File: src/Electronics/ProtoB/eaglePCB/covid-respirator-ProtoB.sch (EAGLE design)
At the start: 18 parts, among them IC2 L7805CV-DG, Q1 VNP35N07-E, T2 BC548

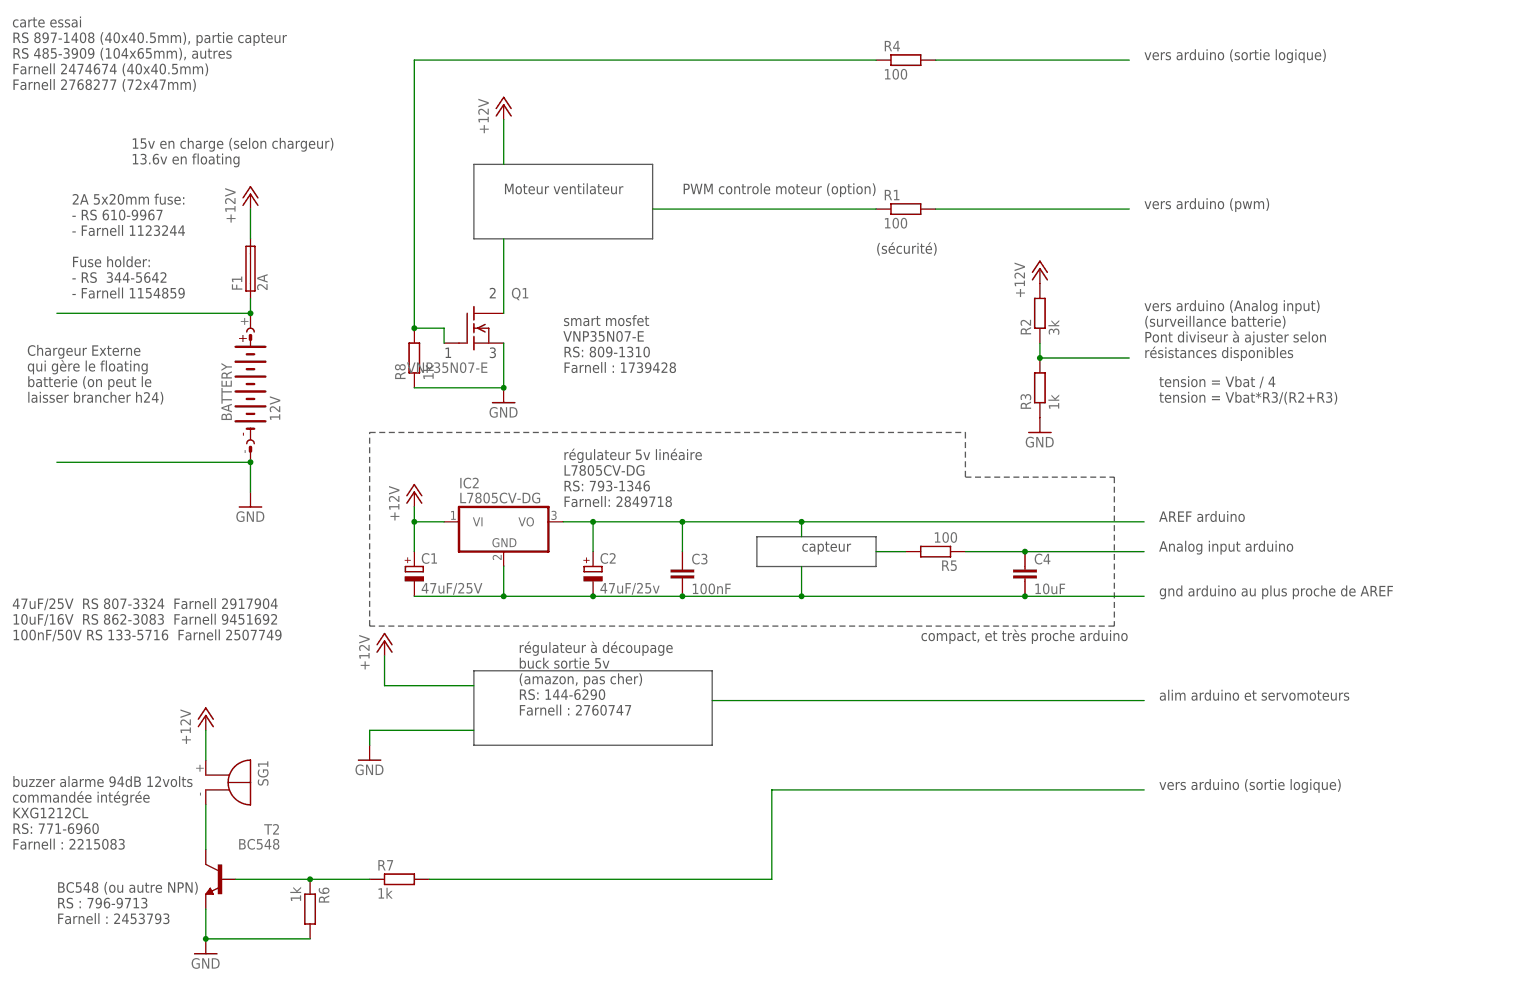
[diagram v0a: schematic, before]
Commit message: update protoB schematic
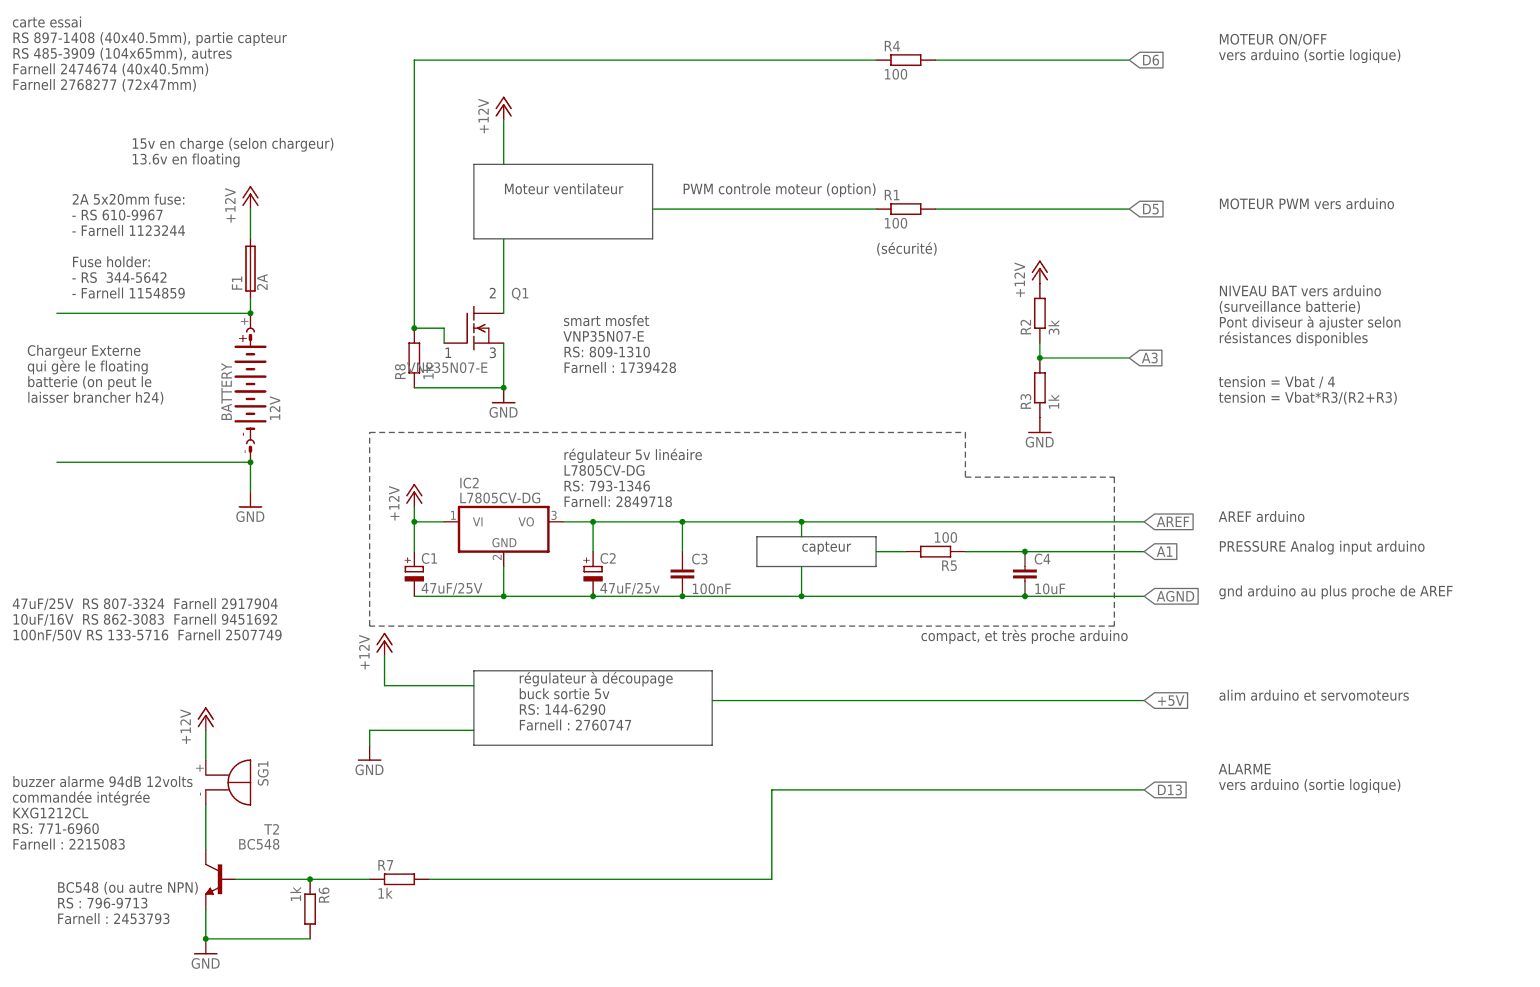
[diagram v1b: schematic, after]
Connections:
- net N$10 renamed A1
- net N$14 renamed D13
- net N$2 renamed D5
- net N$3 renamed A3
- net N$5 renamed D6
- net N$7 renamed AREF
- net N$8 renamed AGND
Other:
- note added: "ALARME vers arduino (sortie logique)"
- note added: "MOTEUR ON/OFF vers arduino (sortie logique)"
- note added: "MOTEUR PWM vers arduino"
- note added: "NIVEAU BAT vers arduino (surveillance batterie) Pont diviseur à ajuster selon résistances disponibles"
- note added: "PRESSURE Analog input arduino"
- note added: "régulateur à découpage buck sortie 5v RS: 144-6290 Farnell : 2760747"
- note removed: "Analog input arduino"
- note removed: "régulateur à découpage buck sortie 5v (amazon, pas cher) RS: 144-6290 Farnell : 2760747"
- note removed: "vers arduino (Analog input) (surveillance batterie) Pont diviseur à ajuster selon résistances disponibles"
- note removed: "vers arduino (pwm)"
- note removed: "vers arduino (sortie logique)"
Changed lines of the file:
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@@
 <text x="73.66" y="83.82" size="1.778" layer="97">PWM controle moteur (option)</text>
 <text x="106.68" y="73.66" size="1.778" layer="97">(sécurité)</text>
-<text x="152.4" y="81.28" size="1.778" layer="97">vers arduino (pwm)</text>
-<text x="152.4" y="55.88" size="1.778" layer="97">vers arduino (Analog input)
+<text x="165.1" y="81.28" size="1.778" layer="97">MOTEUR PWM vers arduino </text>
+<text x="165.1" y="58.42" size="1.778" layer="97">NIVEAU BAT vers arduino
 (surveillance batterie)
 Pont diviseur à ajuster selon
 résistances disponibles</text>
-<text x="154.94" y="48.26" size="1.778" layer="97">tension = Vbat / 4
+<text x="165.1" y="48.26" size="1.778" layer="97">tension = Vbat / 4
 tension = Vbat*R3/(R2+R3)</text>
 <text x="-20.32" y="88.9" size="1.778" layer="97">15v en charge (selon chargeur)
 13.6v en floating</text>
-<text x="152.4" y="106.68" size="1.778" layer="97">vers arduino (sortie logique)</text>
+<text x="165.1" y="106.68" size="1.778" layer="97">MOTEUR ON/OFF
+vers arduino (sortie logique)</text>
 <wire x1="86.36" y1="25.4" x2="106.68" y2="25.4" width="0.1524" layer="97"/>
 <wire x1="106.68" y1="25.4" x2="106.68" y2="20.32" width="0.1524" layer="97"/>
@@
 <wire x1="86.36" y1="20.32" x2="86.36" y2="25.4" width="0.1524" layer="97"/>
 <text x="93.98" y="22.86" size="1.778" layer="97">capteur</text>
-<text x="154.94" y="27.94" size="1.778" layer="97">AREF arduino</text>
-<text x="154.94" y="22.86" size="1.778" layer="97">Analog input arduino</text>
-<text x="154.94" y="15.24" size="1.778" layer="97">gnd arduino au plus proche de AREF</text>
+<text x="165.1" y="27.94" size="1.778" layer="97">AREF arduino</text>
+<text x="165.1" y="22.86" size="1.778" layer="97">PRESSURE Analog input arduino</text>
+<text x="165.1" y="15.24" size="1.778" layer="97">gnd arduino au plus proche de AREF</text>
 <wire x1="38.1" y1="2.54" x2="78.74" y2="2.54" width="0.1524" layer="97"/>
 <wire x1="78.74" y1="2.54" x2="78.74" y2="-10.16" width="0.1524" layer="97"/>
 <wire x1="78.74" y1="-10.16" x2="38.1" y2="-10.16" width="0.1524" layer="97"/>
 <wire x1="38.1" y1="-10.16" x2="38.1" y2="2.54" width="0.1524" layer="97"/>
-<text x="45.72" y="-5.08" size="1.778" layer="97">régulateur à découpage
+<text x="45.72" y="-7.62" size="1.778" layer="97">régulateur à découpage
 buck sortie 5v
-(amazon, pas cher)
 RS: 144-6290
 Farnell : 2760747</text>
-<text x="154.94" y="-2.54" size="1.778" layer="97">alim arduino et servomoteurs</text>
+<text x="165.1" y="-2.54" size="1.778" layer="97">alim arduino et servomoteurs</text>
 <text x="53.34" y="53.34" size="1.778" layer="97">smart mosfet
 VNP35N07-E
@@
 RS: 771-6960
 Farnell : 2215083</text>
-<text x="154.94" y="-17.78" size="1.778" layer="97">vers arduino (sortie logique)</text>
+<text x="165.1" y="-17.78" size="1.778" layer="97">ALARME
+vers arduino (sortie logique)</text>
 <text x="-33.02" y="-40.64" size="1.778" layer="97">BC548 (ou autre NPN)
 RS : 796-9713
@@
 </segment>
 </net>
-<net name="N$2" class="0">
+<net name="D5" class="0">
 <segment>
 <pinref part="R1" gate="G$1" pin="2"/>
 <wire x1="116.84" y1="81.28" x2="149.86" y2="81.28" width="0.1524" layer="91"/>
-</segment>
-</net>
-<net name="N$3" class="0">
+<label x="149.86" y="81.28" size="1.778" layer="95" xref="yes"/>
+</segment>
+</net>
+<net name="A3" class="0">
 <segment>
 <pinref part="R2" gate="G$1" pin="1"/>
@@
 <wire x1="134.62" y1="55.88" x2="149.86" y2="55.88" width="0.1524" layer="91"/>
 <junction x="134.62" y="55.88"/>
+<label x="149.86" y="55.88" size="1.778" layer="95" xref="yes"/>
 </segment>
 </net>
@@
 </segment>
 </net>
-<net name="N$5" class="0">
+<net name="D6" class="0">
 <segment>
 <pinref part="R4" gate="G$1" pin="2"/>
 <wire x1="116.84" y1="106.68" x2="149.86" y2="106.68" width="0.1524" layer="91"/>
-</segment>
-</net>
-<net name="N$7" class="0">
+<label x="149.86" y="106.68" size="1.778" layer="95" xref="yes"/>
+</segment>
+</net>
+<net name="AREF" class="0">
 <segment>
 <pinref part="IC2" gate="A1" pin="VO"/>
@@
 <wire x1="93.98" y1="27.94" x2="152.4" y2="27.94" width="0.1524" layer="91"/>
 <junction x="93.98" y="27.94"/>
-</segment>
-</net>
-<net name="N$8" class="0">
+<label x="152.4" y="27.94" size="1.778" layer="95" xref="yes"/>
+</segment>
+</net>
+<net name="AGND" class="0">
 <segment>
 <pinref part="C1" gate="G$1" pin="-"/>
@@
 <wire x1="132.08" y1="15.24" x2="152.4" y2="15.24" width="0.1524" layer="91"/>
 <junction x="132.08" y="15.24"/>
+<label x="152.4" y="15.24" size="1.778" layer="95" xref="yes"/>
 </segment>
 </net>
@@
 </segment>
 </net>
-<net name="N$10" class="0">
+<net name="A1" class="0">
 <segment>
 <pinref part="R5" gate="G$1" pin="1"/>
@@
 <wire x1="132.08" y1="22.86" x2="152.4" y2="22.86" width="0.1524" layer="91"/>
 <junction x="132.08" y="22.86"/>
-</segment>
-</net>
-<net name="N$11" class="0">
+<label x="152.4" y="22.86" size="1.778" layer="95" xref="yes"/>
+</segment>
+</net>
+<net name="+5V" class="0">
 <segment>
 <wire x1="78.74" y1="-2.54" x2="152.4" y2="-2.54" width="0.1524" layer="91"/>
+<label x="152.4" y="-2.54" size="1.778" layer="95" xref="yes"/>
 </segment>
 </net>
@@
 </segment>
 </net>
-<net name="N$14" class="0">
+<net name="D13" class="0">
 <segment>
 <pinref part="R7" gate="G$1" pin="2"/>
@@
 <wire x1="88.9" y1="-33.02" x2="88.9" y2="-17.78" width="0.1524" layer="91"/>
 <wire x1="88.9" y1="-17.78" x2="152.4" y2="-17.78" width="0.1524" layer="91"/>
-</segment>
-</net>
+<label x="152.4" y="-17.78" size="1.778" layer="95" xref="yes"/>
+</segment>
+</net>

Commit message: update power supply and sensors
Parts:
- F1: value 2A -> 8A
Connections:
- removed net N$15: BATTERY.+, F1.1
- new net N$2: BATTERY.-
- new net N$3: BATTERY.+
- new net N$5: F1.1
- net GND: no longer BATTERY.-
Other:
- note added: "10A 5x20mm slow fuse: - RS 563-429 Fuse holder: - RS 344-5642 - Farnell 1154859"
- note added: "13.8v power supply that handle battery RS: 740-5001"
- note added: "B+"
- note added: "B-"
- note added: "L"
- note added: "NIVEAU BAT vers arduino (<13.5v => perte 220v) Pont diviseur à ajuster selon résistances disponibles"
- note added: "V+"
- note added: "V-"
- note removed: "2A 5x20mm fuse: - RS 610-9967 - Farnell 1123244 Fuse holder: - RS 344-5642 - Farnell 1154859"
- note removed: "Chargeur Externe qui gère le floating batterie (on peut le laisser brancher h24)"
- note removed: "NIVEAU BAT vers arduino (surveillance batterie) Pont diviseur à ajuster selon résistances disponibles"
- moved on the sheet: BATTERY, F1
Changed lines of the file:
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@@
 <part name="R7" library="rcl" deviceset="R-EU_" device="0207/10" value="1k"/>
 <part name="R8" library="rcl" deviceset="R-EU_" device="0207/10" value="1k"/>
-<part name="F1" library="fuse" deviceset="19560" device="" value="2A"/>
+<part name="F1" library="fuse" deviceset="19560" device="" value="8A"/>
 </parts>
 <sheets>
 <sheet>
 <plain>
-<text x="-38.1" y="48.26" size="1.778" layer="97">Chargeur Externe
-qui gère le floating
-batterie (on peut le
-laisser brancher h24)</text>
 <wire x1="38.1" y1="88.9" x2="68.58" y2="88.9" width="0.1524" layer="97"/>
 <wire x1="68.58" y1="88.9" x2="68.58" y2="76.2" width="0.1524" layer="97"/>
@@
 <text x="165.1" y="81.28" size="1.778" layer="97">MOTEUR PWM vers arduino </text>
 <text x="165.1" y="58.42" size="1.778" layer="97">NIVEAU BAT vers arduino
-(surveillance batterie)
+(&lt;13.5v =&gt; perte 220v)
 Pont diviseur à ajuster selon
 résistances disponibles</text>
 <text x="165.1" y="48.26" size="1.778" layer="97">tension = Vbat / 4
 tension = Vbat*R3/(R2+R3)</text>
-<text x="-20.32" y="88.9" size="1.778" layer="97">15v en charge (selon chargeur)
+<text x="-20.32" y="93.98" size="1.778" layer="97">15v en charge (selon chargeur)
 13.6v en floating</text>
 <text x="165.1" y="106.68" size="1.778" layer="97">MOTEUR ON/OFF
@@
 100nF/50V RS 133-5716  Farnell 2507749
 </text>
-<text x="-30.48" y="66.04" size="1.778" layer="97">2A 5x20mm fuse:
-- RS 610-9967
-- Farnell 1123244
+<text x="-30.48" y="73.66" size="1.778" layer="97">10A 5x20mm slow fuse:
+- RS 563-429
 Fuse holder:
 - RS  344-5642
 - Farnell 1154859</text>
+<wire x1="-40.64" y1="58.42" x2="-12.7" y2="58.42" width="0.1524" layer="97"/>
+<wire x1="-12.7" y1="58.42" x2="-12.7" y2="40.64" width="0.1524" layer="97"/>
+<wire x1="-12.7" y1="40.64" x2="-40.64" y2="40.64" width="0.1524" layer="97"/>
+<wire x1="-40.64" y1="40.64" x2="-40.64" y2="58.42" width="0.1524" layer="97"/>
+<text x="-39.37" y="46.99" size="1.778" layer="97">13.8v power supply
+that handle battery
+RS: 740-5001</text>
+<text x="-30.48" y="41.91" size="1.778" layer="97">B-</text>
+<text x="-20.32" y="41.91" size="1.778" layer="97">B+</text>
+<text x="-16.51" y="55.88" size="1.778" layer="97">V+</text>
+<text x="-16.51" y="44.45" size="1.778" layer="97">V-</text>
+<text x="-15.24" y="49.53" size="1.778" layer="97">L</text>
 </plain>
 <instances>
-<instance part="BATTERY" gate="G$1" x="0" y="50.8" rot="R90"/>
-<instance part="P+1" gate="1" x="0" y="83.82"/>
-<instance part="GND1" gate="1" x="0" y="30.48"/>
+<instance part="BATTERY" gate="G$1" x="-22.86" y="30.48"/>
+<instance part="P+1" gate="1" x="2.54" y="91.44"/>
+<instance part="GND1" gate="1" x="0" y="38.1"/>
 <instance part="P+2" gate="1" x="43.18" y="99.06"/>
 <instance part="GND2" gate="1" x="43.18" y="48.26"/>
@@
 <instance part="R7" gate="G$1" x="25.4" y="-33.02"/>
 <instance part="R8" gate="G$1" x="27.94" y="55.88" rot="R90"/>
-<instance part="F1" gate="F" x="0" y="71.12" rot="R90"/>
+<instance part="F1" gate="F" x="2.54" y="76.2" rot="R90"/>
 </instances>
 <busses>
@@
 <nets>
 <net name="GND" class="0">
-<segment>
-<pinref part="BATTERY" gate="G$1" pin="-"/>
-<wire x1="0" y1="38.1" x2="-33.02" y2="38.1" width="0.1524" layer="91"/>
-<pinref part="GND1" gate="1" pin="GND"/>
-<wire x1="0" y1="38.1" x2="0" y2="33.02" width="0.1524" layer="91"/>
-<junction x="0" y="38.1"/>
-</segment>
 <segment>
 <pinref part="GND3" gate="1" pin="GND"/>
@@
 <wire x1="10.16" y1="-43.18" x2="-7.62" y2="-43.18" width="0.1524" layer="91"/>
 <junction x="-7.62" y="-43.18"/>
+</segment>
+<segment>
+<pinref part="GND1" gate="1" pin="GND"/>
+<wire x1="-12.7" y1="45.72" x2="0" y2="45.72" width="0.1524" layer="91"/>
+<wire x1="0" y1="45.72" x2="0" y2="40.64" width="0.1524" layer="91"/>
 </segment>
 </net>
@@
 <pinref part="F1" gate="F" pin="2"/>
 <pinref part="P+1" gate="1" pin="+12V"/>
-<wire x1="0" y1="76.2" x2="0" y2="81.28" width="0.1524" layer="91"/>
+<wire x1="2.54" y1="81.28" x2="2.54" y2="88.9" width="0.1524" layer="91"/>
 </segment>
 </net>
@@
 </segment>
 </net>
-<net name="N$15" class="0">
-<segment>
+<net name="N$2" class="0">
+<segment>
+<wire x1="-30.48" y1="40.64" x2="-30.48" y2="38.1" width="0.1524" layer="91"/>
+<pinref part="BATTERY" gate="G$1" pin="-"/>
+<wire x1="-30.48" y1="38.1" x2="-35.56" y2="38.1" width="0.1524" layer="91"/>
+<wire x1="-35.56" y1="38.1" x2="-35.56" y2="30.48" width="0.1524" layer="91"/>
+</segment>
+</net>
+<net name="N$3" class="0">
+<segment>
+<wire x1="-20.32" y1="40.64" x2="-20.32" y2="38.1" width="0.1524" layer="91"/>
 <pinref part="BATTERY" gate="G$1" pin="+"/>
-<wire x1="0" y1="63.5" x2="-33.02" y2="63.5" width="0.1524" layer="91"/>
+<wire x1="-20.32" y1="38.1" x2="-10.16" y2="38.1" width="0.1524" layer="91"/>
+<wire x1="-10.16" y1="38.1" x2="-10.16" y2="30.48" width="0.1524" layer="91"/>
+</segment>
+</net>
+<net name="N$5" class="0">
+<segment>
+<wire x1="-12.7" y1="55.88" x2="2.54" y2="55.88" width="0.1524" layer="91"/>
 <pinref part="F1" gate="F" pin="1"/>
-<wire x1="0" y1="66.04" x2="0" y2="63.5" width="0.1524" layer="91"/>
-<junction x="0" y="63.5"/>
-</segment>
-</net>
+<wire x1="2.54" y1="71.12" x2="2.54" y2="55.88" width="0.1524" layer="91"/>
+</segment>
+</net>
